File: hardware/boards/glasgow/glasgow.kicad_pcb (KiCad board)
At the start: 4 copper layers, 80 x 49 mm, 272 parts, among them J1 USB_C_USB2.0, J10 AUX, J2 IDC-Header_2x10_P2.54mm, J3 IDC-Header_2x10_P2.54mm, J4 Conn_01x02, J5 PinHeader_2x22_P1.27mm, J6 Conn_01x08, J7 Conn_01x08, J8 Conn_01x08, J9 Conn_01x08, SW1 RST, U1 CY7C68013A-56LTX, U10 SN74LVC1T45DCKR, U11 SN74LVC1T45DCKR, U12 INA233, U13 DAC081C081CIMK, U14 TPS73101DBV, U15 TPD3S014, U16 SN74LVC1T45DCKR, U17 SN74LVC1T45DCKR, U18 SN74LVC1T45DCKR, U19 PCA6408APW, U2 CAT24M01X, U20 DAC081C081CIMK, U21 INA233, U22 SN74LVC1T45DCKR, U23 SN74LVC1T45DCKR, U24 SN74LVC1T45DCKR, U25 SN74LVC1T45DCKR, U26 SN74LVC1T45DCKR, U27 SN74LVC1T45DCKR, U28 SN74LVC1T45DCKR, U29 SN74LVC1T45DCKR, U3 BL24C256A-SFRC, U30 ICE40HX8K-BG121, U31 TPS73101DBV, U32 SN74LVC1T45DCKR, U36 TLV73312PQDRVR, U4 SN74LVC1T45DCKR, U5 PCA6408APW, U6 SN74LVC1T45DCKR, U7 APX811-40UG-7, U8 TLV75533PDRVR, U9 SN74LVC1T45DCKR, Y1 24M

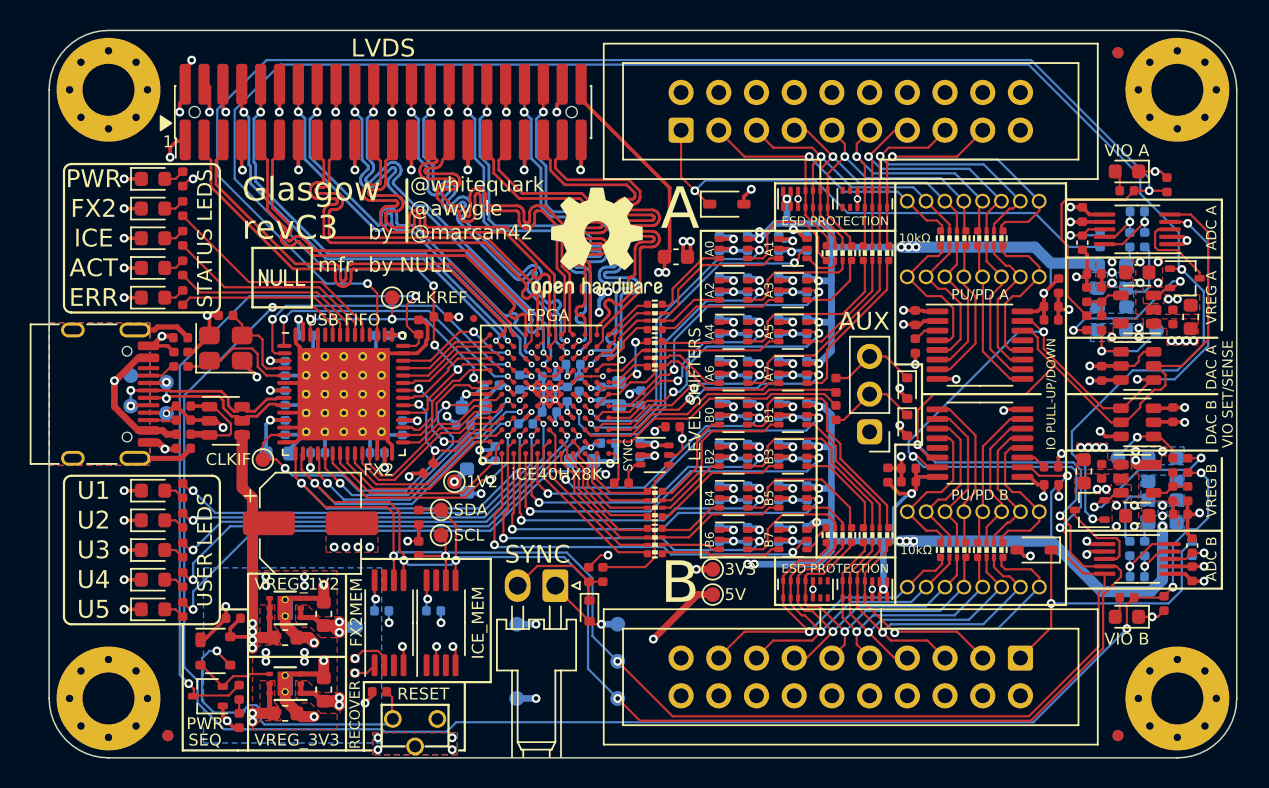
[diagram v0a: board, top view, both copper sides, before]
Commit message: Remove one of the sides
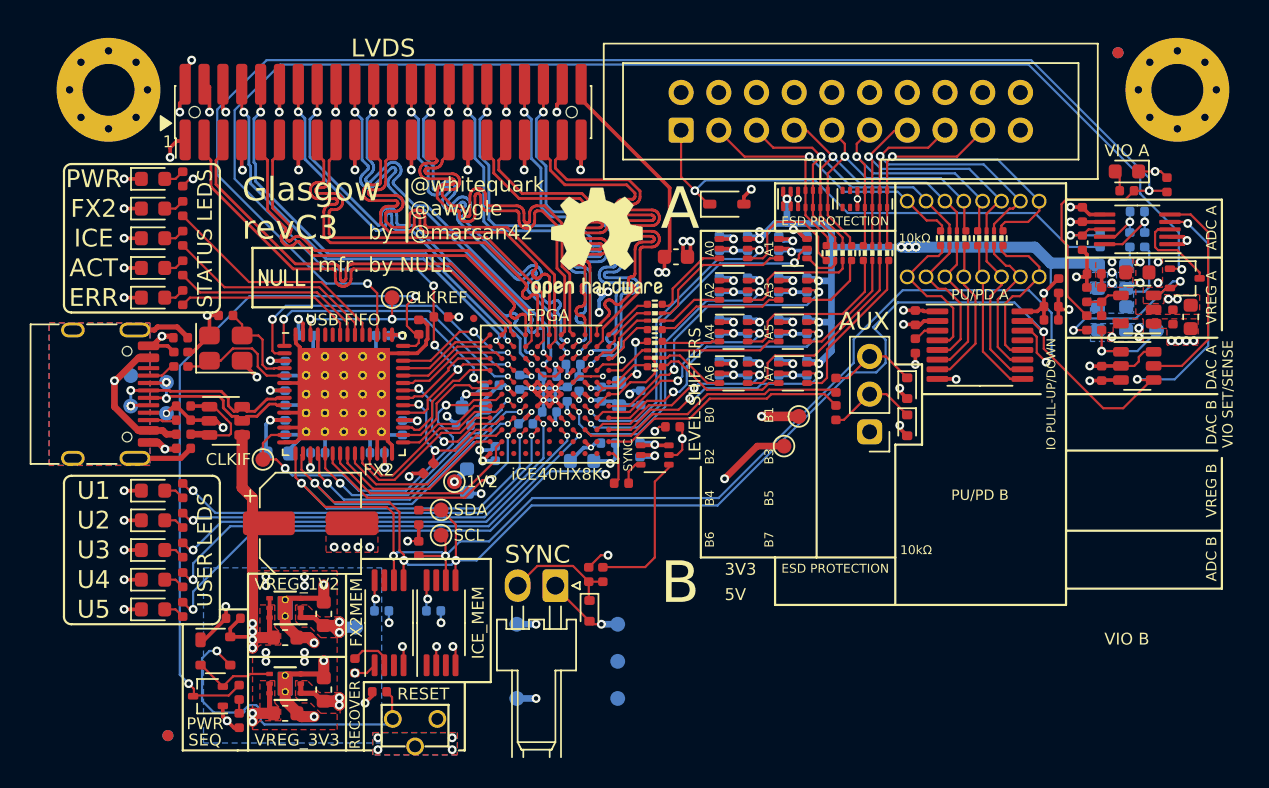
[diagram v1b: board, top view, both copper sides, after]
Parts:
- removed C22, C29, C30, C32, C44, C45, C46, C60, C61, C62, C63, C64, C65, C66, C67, C68, C69, C70, C71, C72, C73, C74, C75: u1, Capacitor_SMD:C_0402_1005Metric
- removed C31, C53: 4u7, Capacitor_SMD:C_0603_1608Metric
- removed C90: 1n 50V C0G, Capacitor_SMD:C_0402_1005Metric
- removed D14: GRN, LED_SMD:LED_0603_1608Metric
- removed D16: CDSOD323-T36S, Glasgow:D_SOD-323
- removed D18: BAT54CW, Glasgow:SOT-323_SC-70
- removed D20, D21: SP3012-06UTG, Glasgow:UDFN-14_3.5x1.35mm_P0.5mm
- removed FID3, FID6: Fiducial_0.75mm_Mask1.5mm, Fiducial:Fiducial_0.75mm_Mask1.5mm
- removed J3: IDC-Header_2x10_P2.54mm, Connector_IDC:IDC-Header_2x10_P2.54mm_Vertical
- removed J6, J7: Conn_01x08, Glasgow:PinSocket_1x08_P1.27mm_Vertical_DNP
- removed MK1, MK4: Mounting_Hole_PAD, Glasgow:MountingHole_3.5mm_Pad_Via_CrtYd
- removed R19, R26, R36: 10k, Resistor_SMD:R_0402_1005Metric
- removed R24, R25: 4R7, Resistor_SMD:R_0402_1005Metric
- removed R27: 49k9, Resistor_SMD:R_0402_1005Metric
- removed R28: 59k, Resistor_SMD:R_0402_1005Metric
- removed R29: 24k3, Resistor_SMD:R_0402_1005Metric
- removed R41, R57: 2k2, Resistor_SMD:R_0402_1005Metric
- removed R46: 20k, Resistor_SMD:R_0402_1005Metric
- removed R48: 0R15, Resistor_SMD:R_0603_1608Metric
- removed R50, R6: DNP, Glasgow:R_0603_1608Metric_DNP
- removed R59: 470, Resistor_SMD:R_0402_1005Metric
- removed R7: 0R33, Resistor_SMD:R_0603_1608Metric
- removed RN1, RN2, RN3, RN4: 33R, Glasgow:R_Array_Convex_4x0402
- removed RN5, RN6: 10k, Glasgow:R_Array_Convex_4x0402
- removed TP18: VDAC, TestPoint:TestPoint_Pad_D1.0mm
- removed U12: INA233, Glasgow:VSSOP-10_3x3mm_P0.5mm
- removed U13: DAC081C081CIMK, Glasgow:SOT-23-6
- removed U14: TPS73101DBV, Glasgow:SOT-23-5
- removed U22, U23, U24, U25, U26, U27, U28, U29: SN74LVC1T45DCKR, Glasgow:SOT-363_SC-70-6
- removed U5: PCA6408APW, Package_SO:TSSOP-16_4.4x5mm_P0.65mm
- moved TP3 11.8 mm to (100.5, 97.0)
- moved TP1 11.1 mm to (99.5, 99.0)
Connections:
- net +1V2 renamed +1V2_glasgow
- net +3V3 renamed +3V3_glasgow
- net +5V renamed +5V_glasgow
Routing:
- net /IO_Banks/VIOB: track 120.4 -> 0.00 mm, vias 19 -> 0
- net /ENVB: track 116.3 -> 0.00 mm, vias 4 -> 0
- net /SCL: track 165.8 -> 113.3 mm, vias 7 -> 5
- net /SDA: track 166.8 -> 120.8 mm, vias 10 -> 7
- net GND: track 255.8 -> 211.5 mm, vias 121 -> 95
- net /IO_Banks/IO_Buffer_B/Z0: track 29.3 -> 0.00 mm, vias 1 -> 0
- net /IO_Banks/DB7: track 28.1 -> 0.00 mm, vias 2 -> 0
- net /IO_Banks/DB5: track 27.5 -> 0.00 mm, vias 2 -> 0
- net /IO_Banks/IO_Buffer_B/Z7: track 26.7 -> 0.00 mm, vias 1 -> 0
- net /IO_Banks/DB3: track 25.9 -> 0.00 mm, vias 2 -> 0
- net /IO_Banks/IO_Buffer_B/Z1: track 25.8 -> 0.00 mm, vias 1 -> 0
- net /IO_Banks/DB6: track 25.5 -> 0.00 mm, vias 2 -> 0
- net /IO_Banks/IO_Buffer_B/Z6: track 24.9 -> 0.00 mm, vias 1 -> 0
- net /~{ALERT}: track 133.8 -> 109.5 mm, vias 5 -> 4
- net /IO_Banks/DB1: track 24.2 -> 0.00 mm, vias 2 -> 0
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- added copper zone on B.Cu, net (none)
- added copper zone on F.Cu, net (none)
- removed copper zone on B.Cu, net /IO_Banks/IO_Buffer_A/ISNS_H
- removed copper zone on B.Cu, net /IO_Banks/IO_Buffer_B/ISNS_H
- removed copper zone on B.Cu, net /IO_Banks/VIOA
- removed copper zone on F.Cu, net /IO_Banks/VIOA
- removed copper zone on B.Cu, net /IO_Banks/VIOB
- removed copper zone on F.Cu, net /IO_Banks/VIOB
- removed copper zone on B.Cu, net Net-(U14-OUT)
- removed copper zone on F.Cu, net Net-(U14-OUT)
- removed copper zone on B.Cu, net Net-(U31-OUT)
- removed copper zone on F.Cu, net Net-(U31-OUT)
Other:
- board outline removed
